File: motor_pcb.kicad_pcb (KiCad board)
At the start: 2 copper layers, 70 x 50 mm, 37 parts, among them J1 Screw_Terminal_01x02, J2 Screw_Terminal_01x02, J3 Conn_01x04, J4 Conn_01x04, J5 Screw_Terminal_01x04, J6 Screw_Terminal_01x04, J7 Conn_01x04, J8 Conn_01x04, U2 A-Star_328PB_Micro, U3 DRV8834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

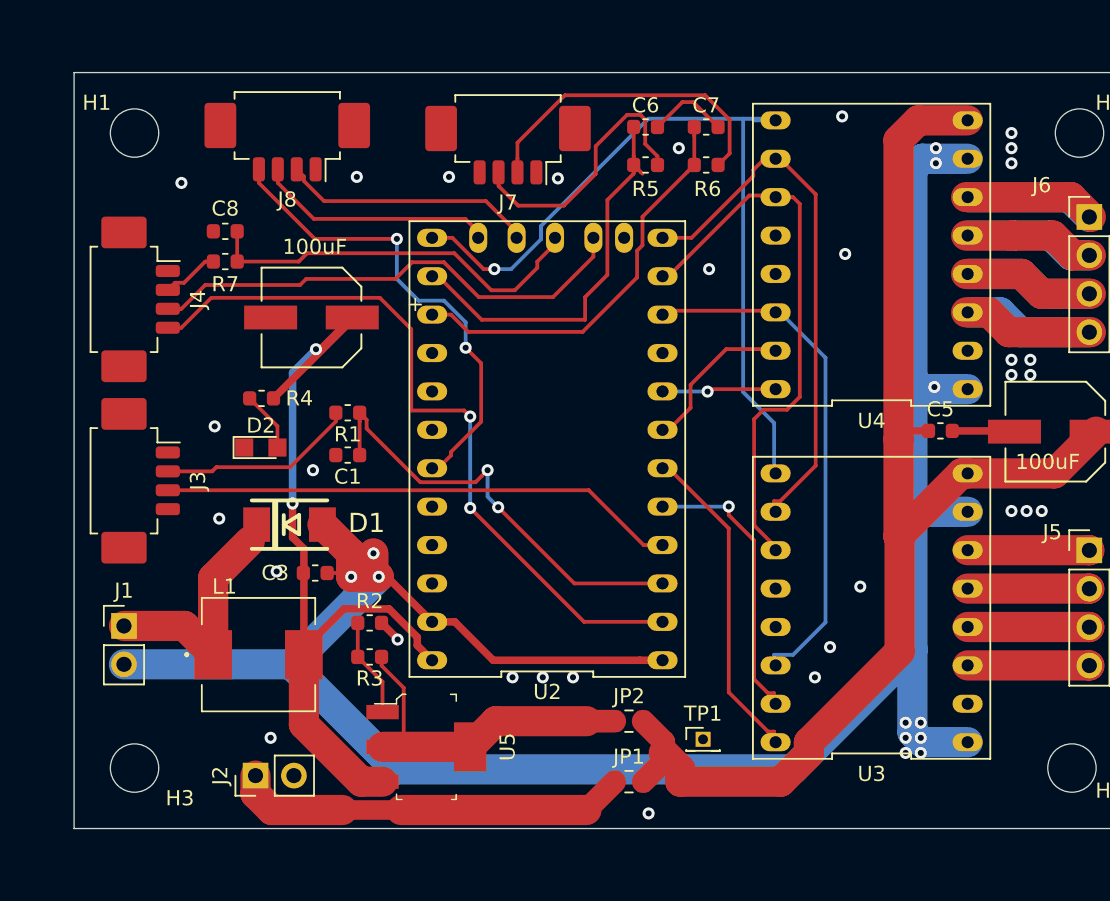
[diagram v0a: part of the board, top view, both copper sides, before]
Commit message: added 5V to sensor connector
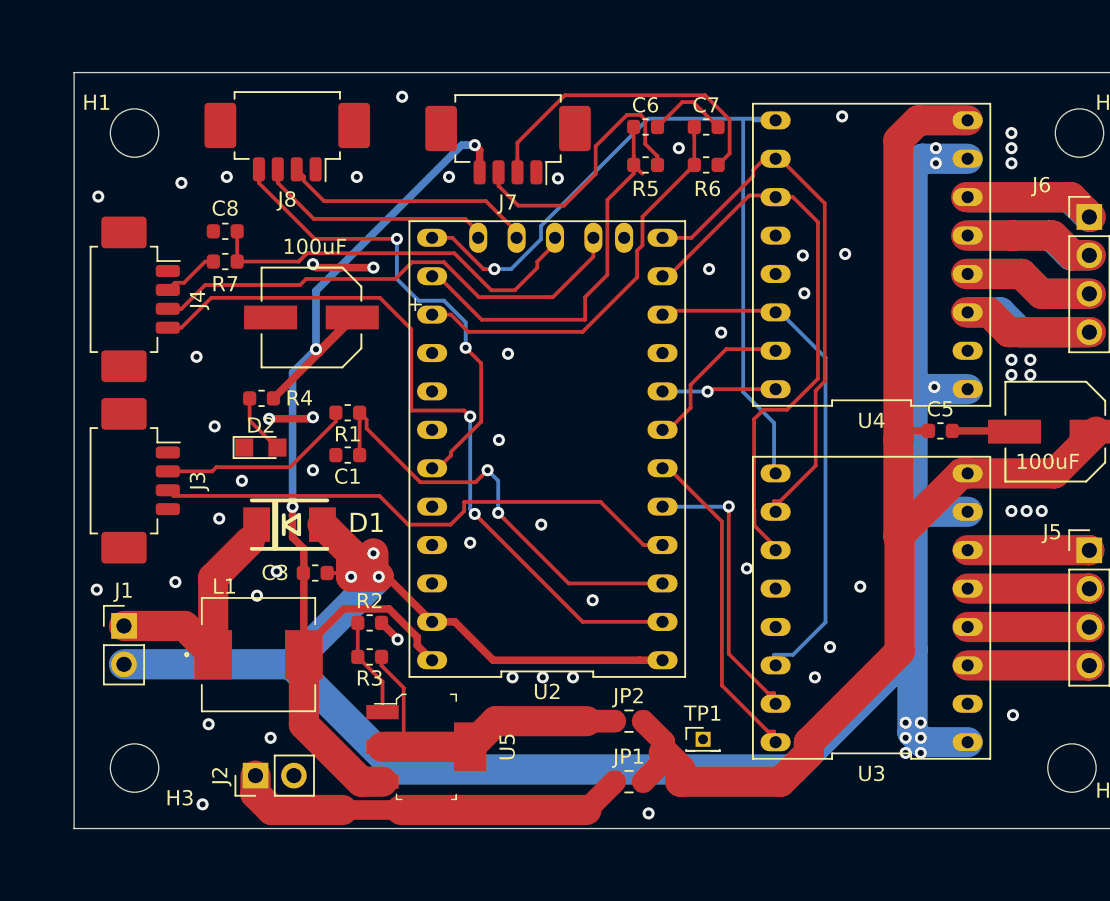
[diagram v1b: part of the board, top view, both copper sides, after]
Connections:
- J7 pad 4: GND -> +5V
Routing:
- net +5V: track 55.0 -> 75.6 mm, vias 2 -> 3
- net GND: track 161.2 -> 168.2 mm, vias 43 -> 67
- net /TXD0: track 34.2 -> 35.8 mm
- net /m1: track 37.0 -> 38.0 mm

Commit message: updated with previously uncommitted changes. Added schematics
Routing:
- net GND: track 168.2 -> 164.5 mm, vias 67 -> 82
- net /~sleep: track 34.5 -> 36.6 mm, vias 0 -> 2
- net /sense1_filt: track 26.2 -> 25.4 mm
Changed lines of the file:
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@@
     (thickness 1.6)
     (drawings 4)
-    (tracks 445)
+    (tracks 464)
     (zones 0)
     (modules 37)
@@
   )
   (setup
-    (last_trace_width 0.5)
+    (last_trace_width 0.25)
     (user_trace_width 0.5)
     (user_trace_width 1.5)
@@
       (outputformat 1)
       (mirror false)
-      (drillshape 1)
+      (drillshape 0)
       (scaleselection 1)
-      (outputdirectory ""))
+      (outputdirectory "outputs/gerber/"))
   )
   (net 0 "")
@@
   (via (at 137 49) (size 0.8) (drill 0.4) (layers F.Cu B.Cu) (net 2))
   (via (at 96.4 67.5) (size 0.8) (drill 0.4) (layers F.Cu B.Cu) (net 2))
-  (segment (start 78.3 69.14) (end 89.36 69.14) (width 2) (layer B.Cu) (net 2))
+  (segment (start 78.3 69.14) (end 80.96 69.14) (width 2) (layer B.Cu) (net 2))
   (via (at 95.15 63.35) (size 0.8) (drill 0.4) (layers F.Cu B.Cu) (net 2))
   (segment (start 89.36 69.14) (end 93.55 64.95) (width 2) (layer B.Cu) (net 2))
@@
   (segment (start 112.42 68.87) (end 113.92 68.87) (width 0.5) (layer F.Cu) (net 2))
   (segment (start 102.72 68.87) (end 112.42 68.87) (width 0.5) (layer F.Cu) (net 2))
-  (segment (start 100.18 66.33) (end 102.72 68.87) (width 0.5) (layer F.Cu) (net 2))
+  (segment (start 100.18 66.33) (end 101.375 67.525) (width 0.5) (layer F.Cu) (net 2))
   (segment (start 98.68 66.33) (end 100.18 66.33) (width 0.5) (layer F.Cu) (net 2))
   (segment (start 122.545588 76.09001) (end 130.45 68.185598) (width 2) (layer B.Cu) (net 2))
@@
   (via (at 130 73) (size 0.8) (drill 0.4) (layers F.Cu B.Cu) (net 2))
   (via (at 131 73) (size 0.8) (drill 0.4) (layers F.Cu B.Cu) (net 2))
-  (via (at 113 79) (size 0.8) (drill 0.4) (layers F.Cu B.Cu) (net 2))
+  (via (at 114 79) (size 0.8) (drill 0.4) (layers F.Cu B.Cu) (net 2))
   (via (at 106 70) (size 0.8) (drill 0.4) (layers F.Cu B.Cu) (net 2))
   (via (at 108 70) (size 0.8) (drill 0.4) (layers F.Cu B.Cu) (net 2))
@@
   (via (at 127 64) (size 0.8) (drill 0.4) (layers F.Cu B.Cu) (net 2))
   (via (at 115 35) (size 0.8) (drill 0.4) (layers F.Cu B.Cu) (net 2))
-  (segment (start 115.9475 31.95) (end 117.135888 33.138388) (width 0.25) (layer F.Cu) (net 2))
-  (segment (start 113.5875 33.6) (end 115.2375 31.95) (width 0.25) (layer F.Cu) (net 2))
-  (segment (start 115.2375 31.95) (end 115.9475 31.95) (width 0.25) (layer F.Cu) (net 2))
   (segment (start 117.135888 33.138388) (end 117.5975 33.6) (width 0.25) (layer F.Cu) (net 2))
   (via (at 107 37) (size 0.8) (drill 0.4) (layers F.Cu B.Cu) (net 2))
@@
   (via (at 83.9 73.1) (size 0.8) (drill 0.4) (layers F.Cu B.Cu) (net 2))
   (via (at 83.5 78.4) (size 0.8) (drill 0.4) (layers F.Cu B.Cu) (net 2))
+  (via (at 119.4 65.8) (size 0.8) (drill 0.4) (layers F.Cu B.Cu) (net 2))
+  (segment (start 117.135888 33.138388) (end 117.135888 33.135888) (width 0.25) (layer F.Cu) (net 2))
+  (segment (start 117.135888 33.135888) (end 116.4 32.4) (width 0.25) (layer F.Cu) (net 2))
+  (via (at 76.8 70.9) (size 0.8) (drill 0.4) (layers F.Cu B.Cu) (net 2))
+  (via (at 80.4 70.6) (size 0.8) (drill 0.4) (layers F.Cu B.Cu) (net 2))
+  (segment (start 80.96 69.14) (end 89.36 69.14) (width 2) (layer B.Cu) (net 2))
+  (via (at 80.96 69.14) (size 0.8) (drill 0.4) (layers F.Cu B.Cu) (net 2))
+  (via (at 111.4 48) (size 0.8) (drill 0.4) (layers F.Cu B.Cu) (net 2))
+  (via (at 118.5 52.6) (size 0.8) (drill 0.4) (layers F.Cu B.Cu) (net 2))
+  (via (at 117.3 55.9) (size 0.8) (drill 0.4) (layers F.Cu B.Cu) (net 2))
+  (via (at 111.1 54.8) (size 0.8) (drill 0.4) (layers F.Cu B.Cu) (net 2))
+  (via (at 127 50.1) (size 0.8) (drill 0.4) (layers F.Cu B.Cu) (net 2))
+  (via (at 136.4 78.2) (size 0.8) (drill 0.4) (layers F.Cu B.Cu) (net 2))
+  (segment (start 101.375 67.525) (end 102.72 68.87) (width 0.5) (layer F.Cu) (net 2))
+  (via (at 101.375 67.525) (size 0.8) (drill 0.4) (layers F.Cu B.Cu) (net 2))
+  (via (at 123.3 78.3) (size 0.8) (drill 0.4) (layers F.Cu B.Cu) (net 2))
+  (via (at 85.1 78.8) (size 0.8) (drill 0.4) (layers F.Cu B.Cu) (net 2))
+  (via (at 84.3 77.4) (size 0.8) (drill 0.4) (layers F.Cu B.Cu) (net 2))
+  (via (at 110.9 79) (size 0.8) (drill 0.4) (layers F.Cu B.Cu) (net 2))
   (segment (start 87 77.7) (end 88.07499 78.77499) (width 2) (layer F.Cu) (net 3))
   (segment (start 87 76.5) (end 87 77.7) (width 2) (layer F.Cu) (net 3))
@@
   (segment (start 114.178 45.752) (end 113.92 46.01) (width 0.25) (layer F.Cu) (net 20))
   (segment (start 121.174 45.752) (end 114.178 45.752) (width 0.25) (layer F.Cu) (net 20))
-  (segment (start 121.7 45.86) (end 121.3 45.86) (width 0.25) (layer B.Cu) (net 20))
-  (segment (start 124.7 48.86) (end 121.7 45.86) (width 0.25) (layer B.Cu) (net 20))
-  (segment (start 124.7 66.36) (end 124.7 48.86) (width 0.25) (layer B.Cu) (net 20))
-  (segment (start 121.3 68.51) (end 122.55 68.51) (width 0.25) (layer B.Cu) (net 20))
-  (segment (start 122.55 68.51) (end 124.7 66.36) (width 0.25) (layer B.Cu) (net 20))
-  (segment (start 121.3 69.11) (end 121.4 69.21) (width 0.25) (layer B.Cu) (net 20))
-  (segment (start 121.3 68.51) (end 121.3 69.11) (width 0.25) (layer B.Cu) (net 20))
+  (via (at 123.3 46.3) (size 0.8) (drill 0.4) (layers F.Cu B.Cu) (net 20))
+  (segment (start 121.4 45.86) (end 122.86 45.86) (width 0.25) (layer F.Cu) (net 20))
+  (segment (start 122.86 45.86) (end 123.3 46.3) (width 0.25) (layer F.Cu) (net 20))
+  (via (at 125.6 46.3) (size 0.8) (drill 0.4) (layers F.Cu B.Cu) (net 20))
+  (segment (start 123.3 46.3) (end 125.6 46.3) (width 0.25) (layer B.Cu) (net 20))
+  (segment (start 124.50002 51.222801) (end 124.50002 56.49998) (width 0.25) (layer F.Cu) (net 20))
+  (segment (start 125.6 46.3) (end 125.6 50.122821) (width 0.25) (layer F.Cu) (net 20))
+  (segment (start 125.6 50.122821) (end 124.50002 51.222801) (width 0.25) (layer F.Cu) (net 20))
+  (segment (start 121.8 69.21) (end 121.4 69.21) (width 0.25) (layer F.Cu) (net 20))
+  (segment (start 122.72501 68.28499) (end 121.8 69.21) (width 0.25) (layer F.Cu) (net 20))
+  (segment (start 122.72501 58.27499) (end 122.72501 68.28499) (width 0.25) (layer F.Cu) (net 20))
+  (segment (start 124.50002 56.49998) (end 122.72501 58.27499) (width 0.25) (layer F.Cu) (net 20))
   (segment (start 116.75 51.09) (end 113.92 51.09) (width 0.25) (layer B.Cu) (net 23))
   (segment (start 121.3 50.94) (end 117.06 50.94) (width 0.25) (layer F.Cu) (net 23))
@@
   (segment (start 98.68 43.47) (end 99.08 43.47) (width 0.25) (layer F.Cu) (net 43))
   (segment (start 101.96 46.35) (end 108.8 46.35) (width 0.25) (layer F.Cu) (net 43))
-  (segment (start 112.474112 36.571612) (end 112.0125 36.11) (width 0.25) (layer F.Cu) (net 43))
-  (segment (start 112.59499 36.69249) (end 112.474112 36.571612) (width 0.25) (layer F.Cu) (net 43))
   (segment (start 112.0125 35.535) (end 112.0125 33.6) (width 0.25) (layer F.Cu) (net 43))
   (segment (start 112.0125 36.11) (end 112.0125 35.535) (width 0.25) (layer F.Cu) (net 43))
